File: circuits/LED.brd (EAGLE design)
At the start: 100 x 80 mm, 17 parts, among them X1 2516-

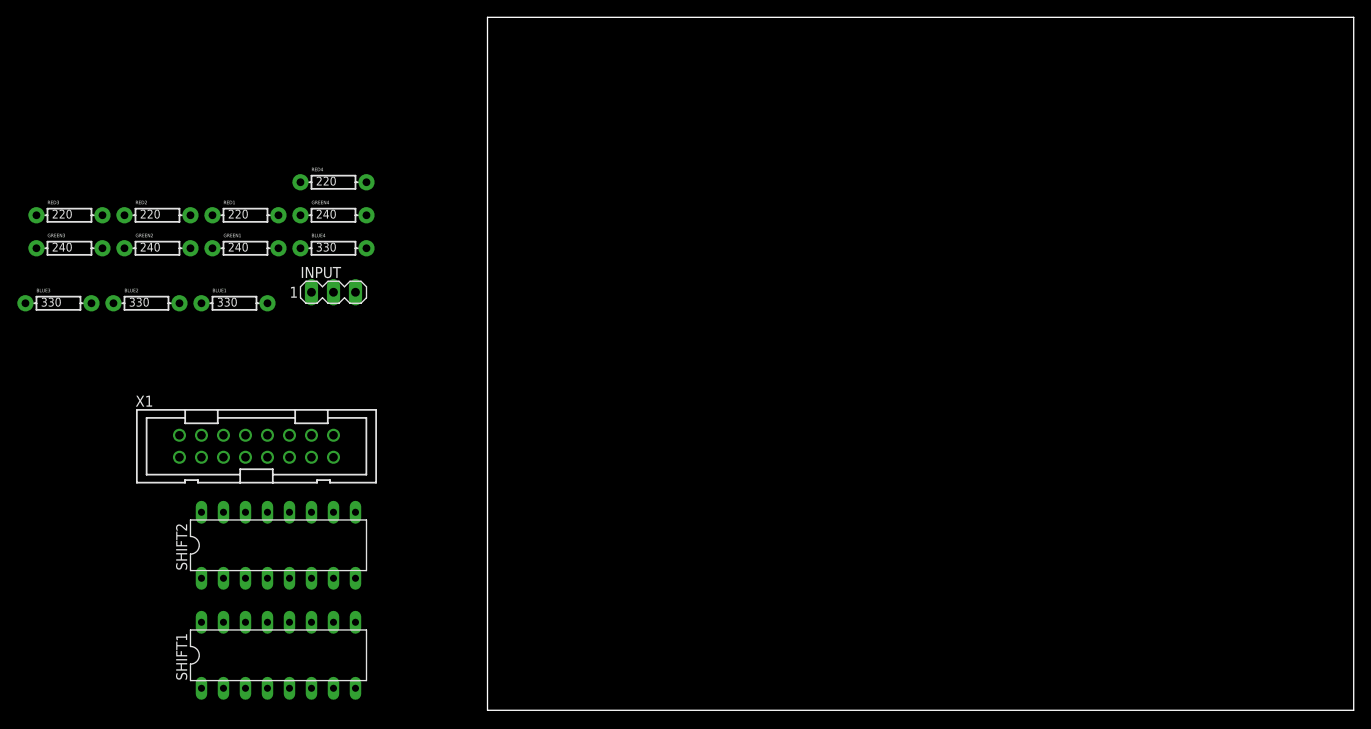
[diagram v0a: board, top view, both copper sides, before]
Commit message: Fix schematic & lay out board
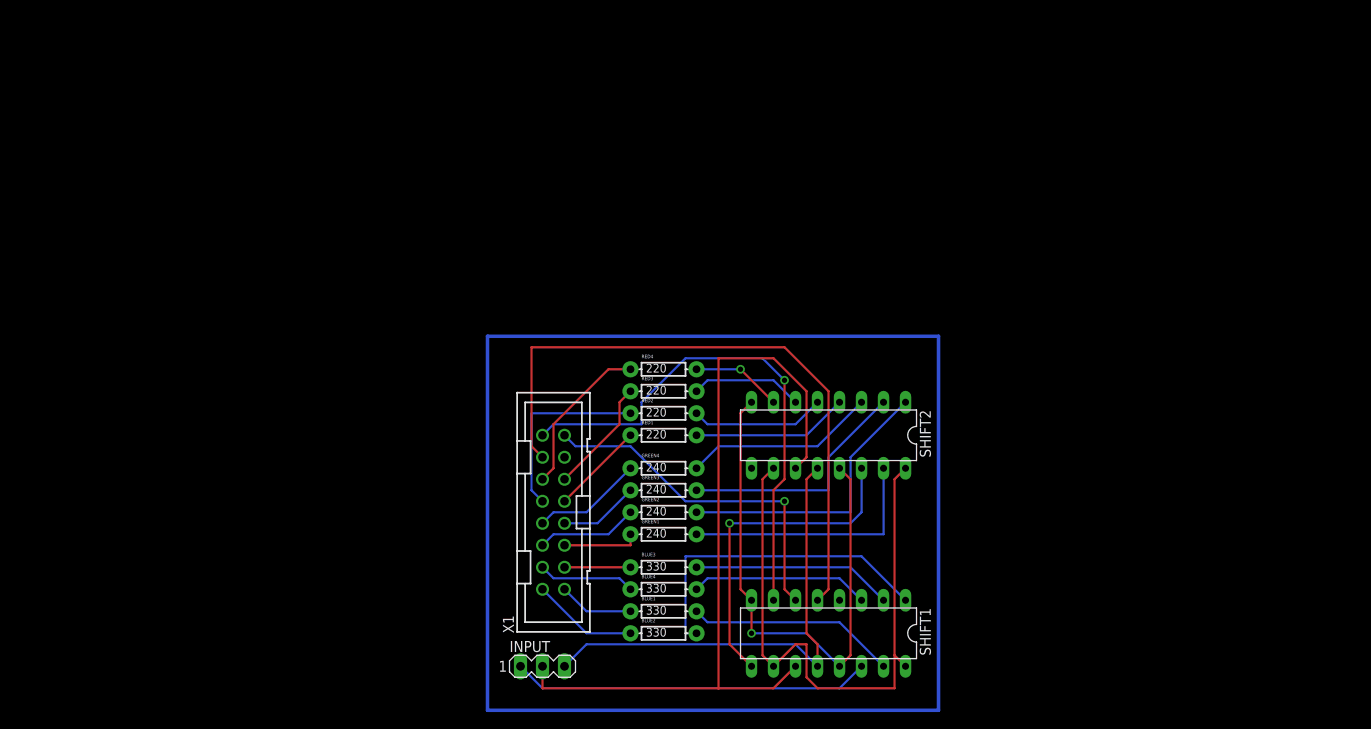
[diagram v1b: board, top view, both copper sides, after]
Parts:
- moved BLUE3 76.2 mm to (20.3, 16.5)
- moved GREEN3 74.1 mm to (20.3, 25.4)
- moved RED3 71.5 mm to (20.3, 36.8)
- moved BLUE2 70.8 mm to (20.3, 8.89)
- moved GREEN2 65.9 mm to (20.3, 22.9)
- moved SHIFT2 64.8 mm to (39.4, 31.8), turned to 180 degrees
- moved SHIFT1 63.6 mm to (39.4, 8.89), turned to 180 degrees
- moved RED2 62.7 mm to (20.3, 34.3)
- moved BLUE1 61.0 mm to (20.3, 11.4)
- moved GREEN1 58.5 mm to (20.3, 20.3)
- moved BLUE4 54.8 mm to (20.3, 14.0)
- moved RED1 54.5 mm to (20.3, 31.8)
- moved INPUT 49.5 mm to (6.35, 5.08)
- moved GREEN4 48.0 mm to (20.3, 27.9)
- moved RED4 43.8 mm to (20.3, 39.4)
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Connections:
- net N$13: now also GREEN1.P$1
- net N$16: now also GREEN4.P$1
- net N$17: now also RED1.P$1
- net N$18: now also RED2.P$1
- net N$26: now also SHIFT2.5
- net N$27: now also SHIFT2.6
- net N$28: now also SHIFT2.7
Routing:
- net N$33: track 0.00 -> 190.5 mm
- net N$30: track 0.00 -> 92.1 mm
- net N$11: track 0.00 -> 74.3 mm
- net VCC: track 0.00 -> 71.0 mm
- net GND: track 0.00 -> 63.4 mm, vias 0 -> 1
- net N$9: track 0.00 -> 60.1 mm, vias 0 -> 1
- net N$29: track 0.00 -> 55.2 mm
- net N$31: track 0.00 -> 41.5 mm
- net N$10: track 0.00 -> 40.5 mm, vias 0 -> 1
- net N$32: track 0.00 -> 38.4 mm, vias 0 -> 1
- net N$6: track 0.00 -> 37.7 mm
- net N$22: track 0.00 -> 33.1 mm
- net N$21: track 0.00 -> 29.2 mm
- net N$23: track 0.00 -> 28.0 mm
- net N$5: track 0.00 -> 24.2 mm
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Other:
- board outline removed

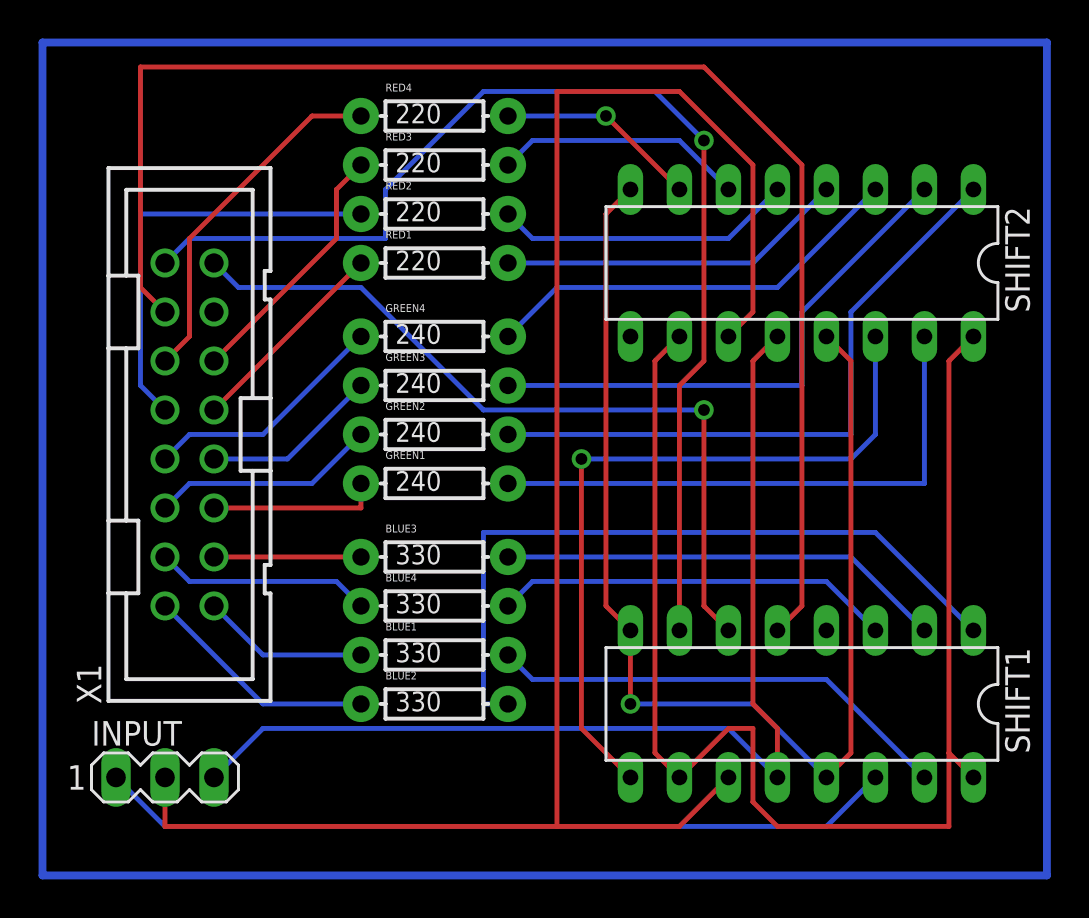
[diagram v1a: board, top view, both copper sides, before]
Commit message: Fix resistor order, add copper pour & version
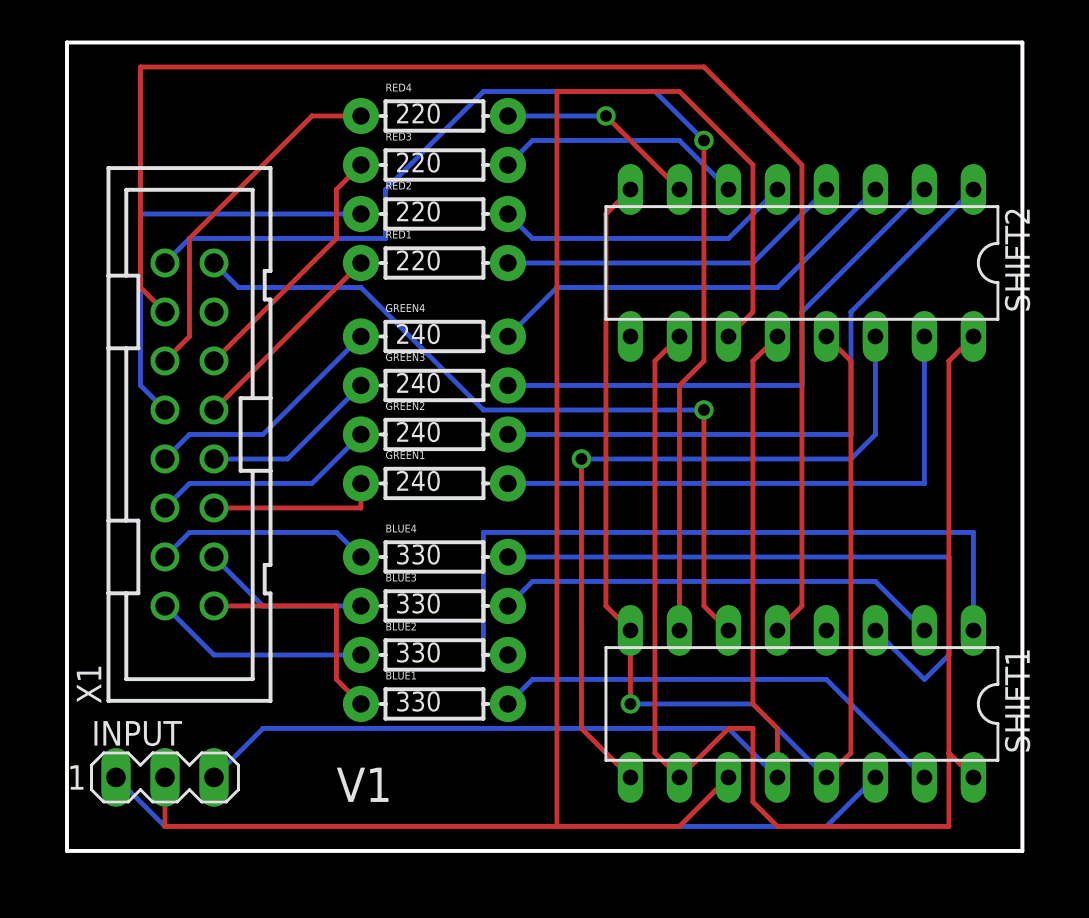
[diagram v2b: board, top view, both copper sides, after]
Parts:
- moved BLUE3 2.54 mm to (20.3, 14.0)
- moved BLUE4 2.54 mm to (20.3, 16.5)
- moved BLUE1 2.54 mm to (20.3, 8.89)
- moved BLUE2 2.54 mm to (20.3, 11.4)
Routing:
- net N$33: track 190.5 -> 0.00 mm
- net N$8: track 20.6 -> 33.3 mm
- net N$4: track 8.67 -> 12.0 mm
- net N$2: track 7.62 -> 8.67 mm
- net N$3: track 12.3 -> 11.2 mm
- added copper zone on layer 1, net GND
- added copper zone on layer 16, net GND
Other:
- board outline added: 49.5 x 41.9 mm
- board text added: "V1"
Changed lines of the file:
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@@
 <board>
 <plain>
+<wire x1="1.27" y1="1.27" x2="1.27" y2="43.18" width="0.2032" layer="20"/>
+<wire x1="1.27" y1="43.18" x2="50.8" y2="43.18" width="0.2032" layer="20"/>
+<wire x1="50.8" y1="43.18" x2="50.8" y2="1.27" width="0.2032" layer="20"/>
+<wire x1="50.8" y1="1.27" x2="1.27" y2="1.27" width="0.2032" layer="20"/>
+<text x="15.24" y="3.81" size="1.778" layer="21">V1</text>
 </plain>
 <attributes>
@@
 <attribute name="OC_FARNELL" value="unknown" x="38.1" y="49.53" size="1.778" layer="27" rot="R90" display="off"/>
 </element>
-<element name="BLUE1" library="SparkFun-Resistors" package="AXIAL-0.3EZ" value="330" x="20.32" y="11.43"/>
-<element name="BLUE2" library="SparkFun-Resistors" package="AXIAL-0.3EZ" value="330" x="20.32" y="8.89"/>
-<element name="BLUE4" library="SparkFun-Resistors" package="AXIAL-0.3EZ" value="330" x="20.32" y="13.97"/>
-<element name="BLUE3" library="SparkFun-Resistors" package="AXIAL-0.3EZ" value="330" x="20.32" y="16.51"/>
+<element name="BLUE1" library="SparkFun-Resistors" package="AXIAL-0.3EZ" value="330" x="20.32" y="8.89"/>
+<element name="BLUE2" library="SparkFun-Resistors" package="AXIAL-0.3EZ" value="330" x="20.32" y="11.43"/>
+<element name="BLUE4" library="SparkFun-Resistors" package="AXIAL-0.3EZ" value="330" x="20.32" y="16.51"/>
+<element name="BLUE3" library="SparkFun-Resistors" package="AXIAL-0.3EZ" value="330" x="20.32" y="13.97"/>
 <element name="GREEN1" library="SparkFun-Resistors" package="AXIAL-0.3EZ" value="240" x="20.32" y="20.32"/>
 <element name="GREEN2" library="SparkFun-Resistors" package="AXIAL-0.3EZ" value="240" x="20.32" y="22.86"/>
@@
 <wire x1="30.48" y1="12.7" x2="30.48" y2="8.89" width="0.254" layer="1"/>
 <via x="30.48" y="8.89" extent="1-16" drill="0.6096"/>
+<polygon width="0.2032" layer="1" isolate="0.3048">
+<vertex x="1.27" y="1.27"/>
+<vertex x="1.27" y="43.18"/>
+<vertex x="50.8" y="43.18"/>
+<vertex x="50.8" y="1.27"/>
+</polygon>
+<polygon width="0.2032" layer="16" isolate="0.3048">
+<vertex x="1.27" y="1.27"/>
+<vertex x="1.27" y="43.18"/>
+<vertex x="50.8" y="43.18"/>
+<vertex x="50.8" y="1.27"/>
+</polygon>
 </signal>
 <signal name="VCC">
@@
 <contactref element="X1" pad="4"/>
 <contactref element="BLUE4" pad="P$1"/>
-<wire x1="7.62" y1="15.24" x2="6.35" y2="16.51" width="0.254" layer="16"/>
-<wire x1="15.24" y1="15.24" x2="7.62" y2="15.24" width="0.254" layer="16"/>
-<wire x1="16.51" y1="13.97" x2="15.24" y2="15.24" width="0.254" layer="16"/>
+<wire x1="7.62" y1="17.78" x2="6.35" y2="16.51" width="0.254" layer="16"/>
+<wire x1="15.24" y1="17.78" x2="7.62" y2="17.78" width="0.254" layer="16"/>
+<wire x1="16.51" y1="16.51" x2="15.24" y2="17.78" width="0.254" layer="16"/>
 </signal>
 <signal name="N$2">
 <contactref element="X1" pad="3"/>
 <contactref element="BLUE3" pad="P$1"/>
-<wire x1="16.51" y1="16.51" x2="8.89" y2="16.51" width="0.254" layer="1"/>
+<wire x1="11.43" y1="13.97" x2="8.89" y2="16.51" width="0.254" layer="16"/>
+<wire x1="16.51" y1="13.97" x2="11.43" y2="13.97" width="0.254" layer="16"/>
 </signal>
 <signal name="N$3">
 <contactref element="X1" pad="2"/>
 <contactref element="BLUE2" pad="P$1"/>
-<wire x1="11.43" y1="8.89" x2="6.35" y2="13.97" width="0.254" layer="16"/>
-<wire x1="16.51" y1="8.89" x2="11.43" y2="8.89" width="0.254" layer="16"/>
+<wire x1="8.89" y1="11.43" x2="6.35" y2="13.97" width="0.254" layer="16"/>
+<wire x1="16.51" y1="11.43" x2="8.89" y2="11.43" width="0.254" layer="16"/>
 </signal>
 <signal name="N$4">
 <contactref element="X1" pad="1"/>
 <contactref element="BLUE1" pad="P$1"/>
-<wire x1="11.43" y1="11.43" x2="8.89" y2="13.97" width="0.254" layer="16"/>
-<wire x1="16.51" y1="11.43" x2="11.43" y2="11.43" width="0.254" layer="16"/>
+<wire x1="15.24" y1="13.97" x2="8.89" y2="13.97" width="0.254" layer="1"/>
+<wire x1="15.24" y1="10.16" x2="15.24" y2="13.97" width="0.254" layer="1"/>
+<wire x1="16.51" y1="8.89" x2="15.24" y2="10.16" width="0.254" layer="1"/>
 </signal>
 <signal name="N$5">
@@
 <contactref element="SHIFT1" pad="15"/>
 <wire x1="40.64" y1="10.16" x2="45.72" y2="5.08" width="0.254" layer="16"/>
-<wire x1="25.4" y1="10.16" x2="40.64" y2="10.16" width="0.254" layer="16"/>
-<wire x1="24.13" y1="11.43" x2="25.4" y2="10.16" width="0.254" layer="16"/>
+<wire x1="25.4" y1="10.16" x2="24.13" y2="8.89" width="0.254" layer="16"/>
+<wire x1="40.64" y1="10.16" x2="25.4" y2="10.16" width="0.254" layer="16"/>
 </signal>
 <signal name="N$6">
 <contactref element="BLUE2" pad="P$2"/>
 <contactref element="SHIFT1" pad="1"/>
-<wire x1="43.18" y1="17.78" x2="48.26" y2="12.7" width="0.254" layer="16"/>
-<wire x1="22.86" y1="17.78" x2="43.18" y2="17.78" width="0.254" layer="16"/>
-<wire x1="22.86" y1="8.89" x2="22.86" y2="17.78" width="0.254" layer="16"/>
-<wire x1="24.13" y1="8.89" x2="22.86" y2="8.89" width="0.254" layer="16"/>
+<wire x1="48.26" y1="17.78" x2="48.26" y2="12.7" width="0.254" layer="16"/>
+<wire x1="22.86" y1="17.78" x2="48.26" y2="17.78" width="0.254" layer="16"/>
+<wire x1="22.86" y1="11.43" x2="22.86" y2="17.78" width="0.254" layer="16"/>
+<wire x1="24.13" y1="11.43" x2="22.86" y2="11.43" width="0.254" layer="16"/>
 </signal>
 <signal name="N$7">
 <contactref element="BLUE3" pad="P$2"/>
 <contactref element="SHIFT1" pad="2"/>
-<wire x1="41.91" y1="16.51" x2="45.72" y2="12.7" width="0.254" layer="16"/>
-<wire x1="24.13" y1="16.51" x2="41.91" y2="16.51" width="0.254" layer="16"/>
+<wire x1="43.18" y1="15.24" x2="45.72" y2="12.7" width="0.254" layer="16"/>
+<wire x1="25.4" y1="15.24" x2="43.18" y2="15.24" width="0.254" layer="16"/>
+<wire x1="24.13" y1="13.97" x2="25.4" y2="15.24" width="0.254" layer="16"/>
 </signal>
 <signal name="N$8">
 <contactref element="BLUE4" pad="P$2"/>
 <contactref element="SHIFT1" pad="3"/>
-<wire x1="40.64" y1="15.24" x2="43.18" y2="12.7" width="0.254" layer="16"/>
-<wire x1="25.4" y1="15.24" x2="40.64" y2="15.24" width="0.254" layer="16"/>
-<wire x1="24.13" y1="13.97" x2="25.4" y2="15.24" width="0.254" layer="16"/>
+<wire x1="45.72" y1="10.16" x2="43.18" y2="12.7" width="0.254" layer="16"/>
+<wire x1="46.99" y1="11.43" x2="45.72" y2="10.16" width="0.254" layer="16"/>
+<wire x1="46.99" y1="16.51" x2="46.99" y2="11.43" width="0.254" layer="16"/>
+<wire x1="24.13" y1="16.51" x2="46.99" y2="16.51" width="0.254" layer="16"/>
 </signal>
 <signal name="N$9">
@@
 <via x="27.94" y="21.59" extent="1-16" drill="0.6096"/>
 </signal>
-<signal name="N$33">
-<wire x1="0" y1="43.18" x2="52.07" y2="43.18" width="0.4064" layer="16"/>
-<wire x1="52.07" y1="43.18" x2="52.07" y2="0" width="0.4064" layer="16"/>
-<wire x1="52.07" y1="0" x2="0" y2="0" width="0.4064" layer="16"/>
-<wire x1="0" y1="0" x2="0" y2="43.18" width="0.4064" layer="16"/>
-</signal>
 </signals>
